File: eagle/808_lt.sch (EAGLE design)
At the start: 54 parts, among them IC1 TL071P, IC2 TL072P, Q1 2N3904, Q2 2N3906, Q3 2N3904, SW8 MSS42_SW_4PDT

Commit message: board started
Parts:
- removed VR10: 100KA, TR808clone:POT_808
- removed VR11: 500R, TR808clone:POT_8089MM
- R216: device TR808clone:R-EU_0207/5V -> TR808clone:R-EU_0207/7
- renumbered R1 to R3, R2 to R4
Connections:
- net GND: now also PINK_NOISE.RING; no longer VR10G$2.C, VR11G$2.C

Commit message: closer
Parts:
- added OUT_NORM, PINK_NORM: 22-23-2021, con-molex:22-23-2021
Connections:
- new net N$3: OUTPUT.NORM, OUT_NORM-1.S
- new net N$4: PINK_NOISE.NORM, PINK_NORM-1.S
- net GND: now also OUT_NORM-2.S, PINK_NORM-2.S, SW8G$4.S; no longer SW8G$2.S
- net N$111: now also SW8G$4.P; no longer SW8G$2.P
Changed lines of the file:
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@@
 <part name="R3" library="pot" deviceset="3RP/1610N" device="" value="100k"/>
 <part name="R4" library="pot" deviceset="3RP/1610N" device="" value="500R"/>
+<part name="PINK_NORM" library="con-molex" deviceset="22-23-2021" device=""/>
+<part name="OUT_NORM" library="con-molex" deviceset="22-23-2021" device=""/>
+<part name="V4" library="supply1" deviceset="GND" device=""/>
+<part name="V5" library="supply1" deviceset="GND" device=""/>
 </parts>
 <sheets>
@@
 <instance part="V54" gate="1" x="22.86" y="50.8"/>
 <instance part="SW8" gate="G$1" x="116.84" y="20.32" rot="MR180"/>
-<instance part="SW8" gate="G$2" x="35.56" y="30.48" rot="MR270"/>
 <instance part="SW8" gate="G$3" x="73.66" y="73.66" rot="MR0"/>
 <instance part="Q1" gate="G1" x="7.62" y="10.16"/>
@@
 <instance part="R3" gate="G$1" x="119.38" y="86.36" rot="R270"/>
 <instance part="R4" gate="G$1" x="38.1" y="71.12" rot="R90"/>
+<instance part="SW8" gate="G$4" x="35.56" y="30.48" rot="MR270"/>
+<instance part="PINK_NORM" gate="-1" x="-12.7" y="10.16" rot="R180"/>
+<instance part="PINK_NORM" gate="-2" x="-12.7" y="12.7" rot="R180"/>
+<instance part="OUT_NORM" gate="-1" x="142.24" y="58.42"/>
+<instance part="OUT_NORM" gate="-2" x="142.24" y="55.88"/>
+<instance part="V4" gate="1" x="-2.54" y="7.62"/>
+<instance part="V5" gate="1" x="137.16" y="50.8"/>
 </instances>
 <busses>
@@
 <pinref part="V159" gate="1" pin="GND"/>
 <wire x1="30.48" y1="25.4" x2="30.48" y2="22.86" width="0.1524" layer="91"/>
-<pinref part="SW8" gate="G$2" pin="S"/>
+<pinref part="SW8" gate="G$4" pin="S"/>
 </segment>
 <segment>
@@
 <pinref part="V3" gate="1" pin="GND"/>
 </segment>
+<segment>
+<pinref part="OUT_NORM" gate="-2" pin="S"/>
+<pinref part="V5" gate="1" pin="GND"/>
+<wire x1="139.7" y1="55.88" x2="137.16" y2="55.88" width="0.1524" layer="91"/>
+<wire x1="137.16" y1="55.88" x2="137.16" y2="53.34" width="0.1524" layer="91"/>
+</segment>
+<segment>
+<pinref part="PINK_NORM" gate="-2" pin="S"/>
+<pinref part="V4" gate="1" pin="GND"/>
+<wire x1="-10.16" y1="12.7" x2="-2.54" y2="12.7" width="0.1524" layer="91"/>
+<wire x1="-2.54" y1="12.7" x2="-2.54" y2="10.16" width="0.1524" layer="91"/>
+</segment>
 </net>
 <net name="N$111" class="0">
@@
 <pinref part="R224" gate="G$1" pin="1"/>
 <wire x1="40.64" y1="27.94" x2="43.18" y2="30.48" width="0.1524" layer="91"/>
-<pinref part="SW8" gate="G$2" pin="P"/>
+<pinref part="SW8" gate="G$4" pin="P"/>
 </segment>
 </net>
@@
 </segment>
 </net>
+<net name="N$3" class="0">
+<segment>
+<pinref part="OUT_NORM" gate="-1" pin="S"/>
+<wire x1="139.7" y1="58.42" x2="137.16" y2="58.42" width="0.1524" layer="91"/>
+<wire x1="137.16" y1="58.42" x2="137.16" y2="76.2" width="0.1524" layer="91"/>
+<pinref part="OUTPUT" gate="G$1" pin="NORM"/>
+<wire x1="137.16" y1="76.2" x2="142.24" y2="76.2" width="0.1524" layer="91"/>
+</segment>
+</net>
+<net name="N$4" class="0">
+<segment>
+<pinref part="PINK_NOISE" gate="G$1" pin="NORM"/>
+<wire x1="-10.16" y1="-2.54" x2="-7.62" y2="-2.54" width="0.1524" layer="91"/>
+<wire x1="-7.62" y1="-2.54" x2="-7.62" y2="10.16" width="0.1524" layer="91"/>
+<pinref part="PINK_NORM" gate="-1" pin="S"/>
+<wire x1="-7.62" y1="10.16" x2="-10.16" y2="10.16" width="0.1524" layer="91"/>
+</segment>
+</net>

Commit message: routed
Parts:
- renumbered R3 to LEVEL, R4 to TUNE
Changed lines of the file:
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@@
 <part name="PINK_NOISE" library="erthenvar" deviceset="AUDIO-JACK" device=""/>
 <part name="V3" library="supply1" deviceset="GND" device=""/>
-<part name="R3" library="pot" deviceset="3RP/1610N" device="" value="100k"/>
-<part name="R4" library="pot" deviceset="3RP/1610N" device="" value="500R"/>
+<part name="LEVEL" library="pot" deviceset="3RP/1610N" device="" value="100k"/>
+<part name="TUNE" library="pot" deviceset="3RP/1610N" device="" value="500R"/>
 <part name="PINK_NORM" library="con-molex" deviceset="22-23-2021" device=""/>
 <part name="OUT_NORM" library="con-molex" deviceset="22-23-2021" device=""/>
@@
 <instance part="PINK_NOISE" gate="G$1" x="-17.78" y="-2.54" rot="MR180"/>
 <instance part="V3" gate="1" x="-10.16" y="-7.62"/>
-<instance part="R3" gate="G$1" x="119.38" y="86.36" rot="R270"/>
-<instance part="R4" gate="G$1" x="38.1" y="71.12" rot="R90"/>
+<instance part="LEVEL" gate="G$1" x="119.38" y="86.36" rot="R270"/>
+<instance part="TUNE" gate="G$1" x="38.1" y="71.12" rot="R90"/>
 <instance part="SW8" gate="G$4" x="35.56" y="30.48" rot="MR270"/>
 <instance part="PINK_NORM" gate="-1" x="-12.7" y="10.16" rot="R180"/>
@@
 <pinref part="D81" gate="G$1" pin="A"/>
 <pinref part="D80" gate="G$1" pin="C"/>
-<pinref part="R4" gate="G$1" pin="A"/>
+<pinref part="TUNE" gate="G$1" pin="A"/>
 </segment>
 </net>
@@
 <wire x1="38.1" y1="78.74" x2="38.1" y2="76.2" width="0.1524" layer="91"/>
 <pinref part="R231" gate="G$1" pin="1"/>
-<pinref part="R4" gate="G$1" pin="S"/>
+<pinref part="TUNE" gate="G$1" pin="S"/>
 </segment>
 </net>
@@
 <pinref part="IC1" gate="A" pin="-IN"/>
 <junction x="114.3" y="50.8"/>
-<pinref part="R3" gate="G$1" pin="A"/>
+<pinref part="LEVEL" gate="G$1" pin="A"/>
 </segment>
 </net>
@@
 <wire x1="119.38" y1="81.28" x2="121.92" y2="81.28" width="0.1524" layer="91"/>
 <pinref part="C82" gate="G$1" pin="-"/>
-<pinref part="R3" gate="G$1" pin="S"/>
+<pinref part="LEVEL" gate="G$1" pin="S"/>
 </segment>
 </net>
@@
 <wire x1="33.02" y1="71.12" x2="30.48" y2="71.12" width="0.1524" layer="91"/>
 <pinref part="V148" gate="1" pin="GND"/>
-<pinref part="R4" gate="G$1" pin="E"/>
-</segment>
-<segment>
+<pinref part="TUNE" gate="G$1" pin="E"/>
+</segment>
+<segment>

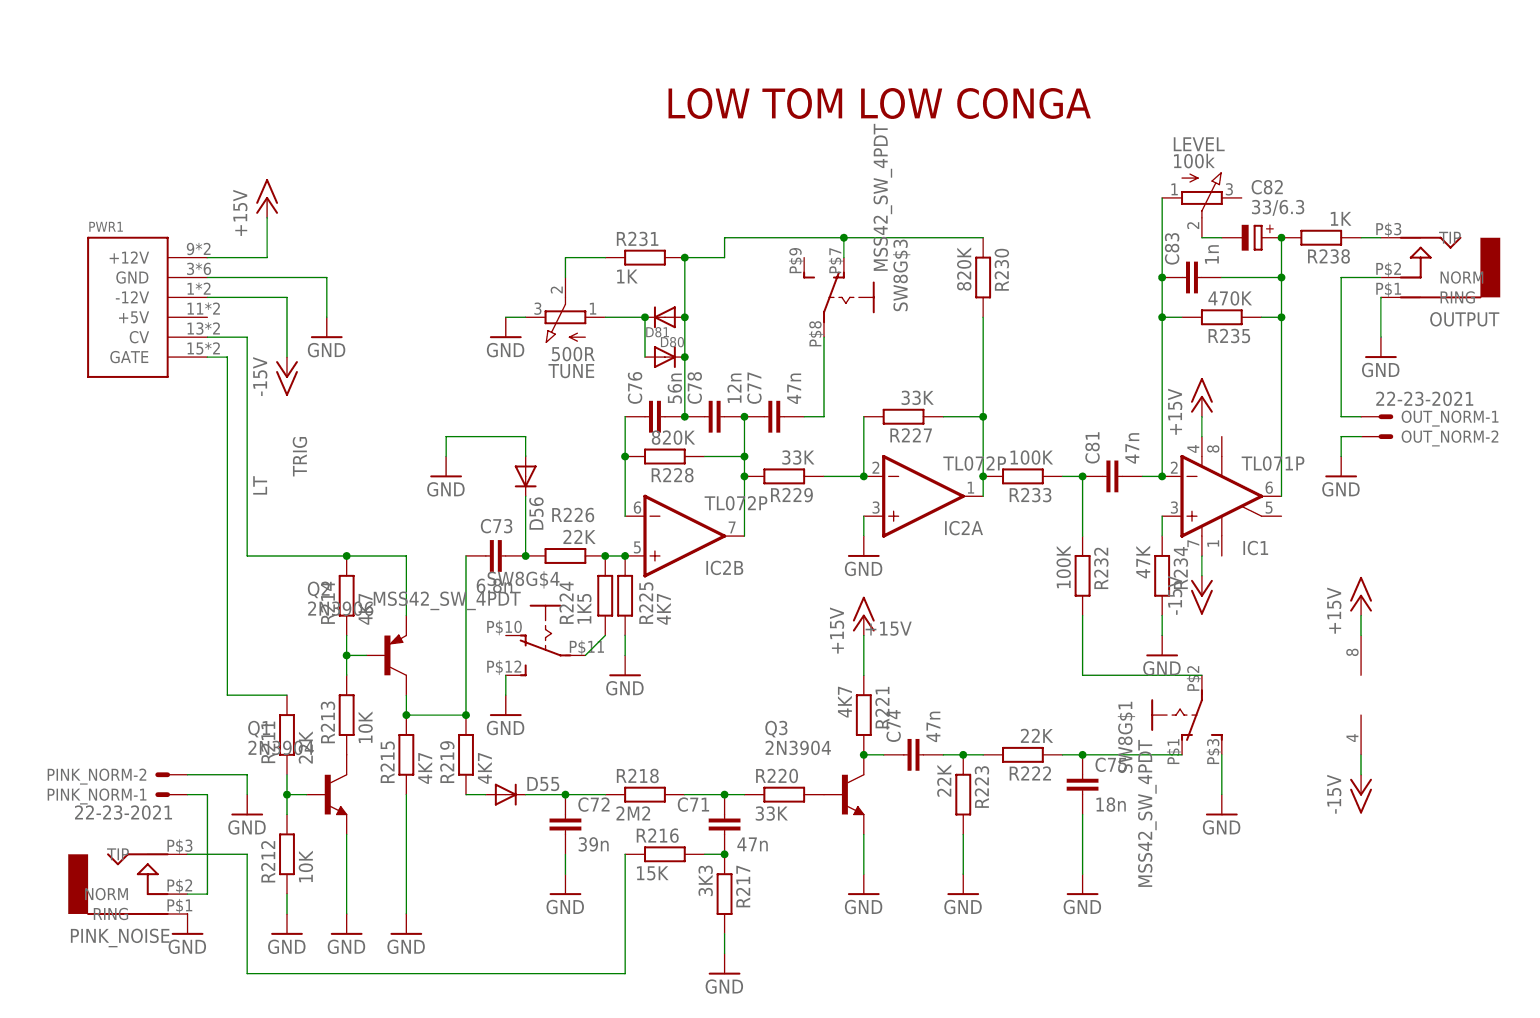
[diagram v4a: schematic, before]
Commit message: corrected 071 power and added resistors to tune pot for value change
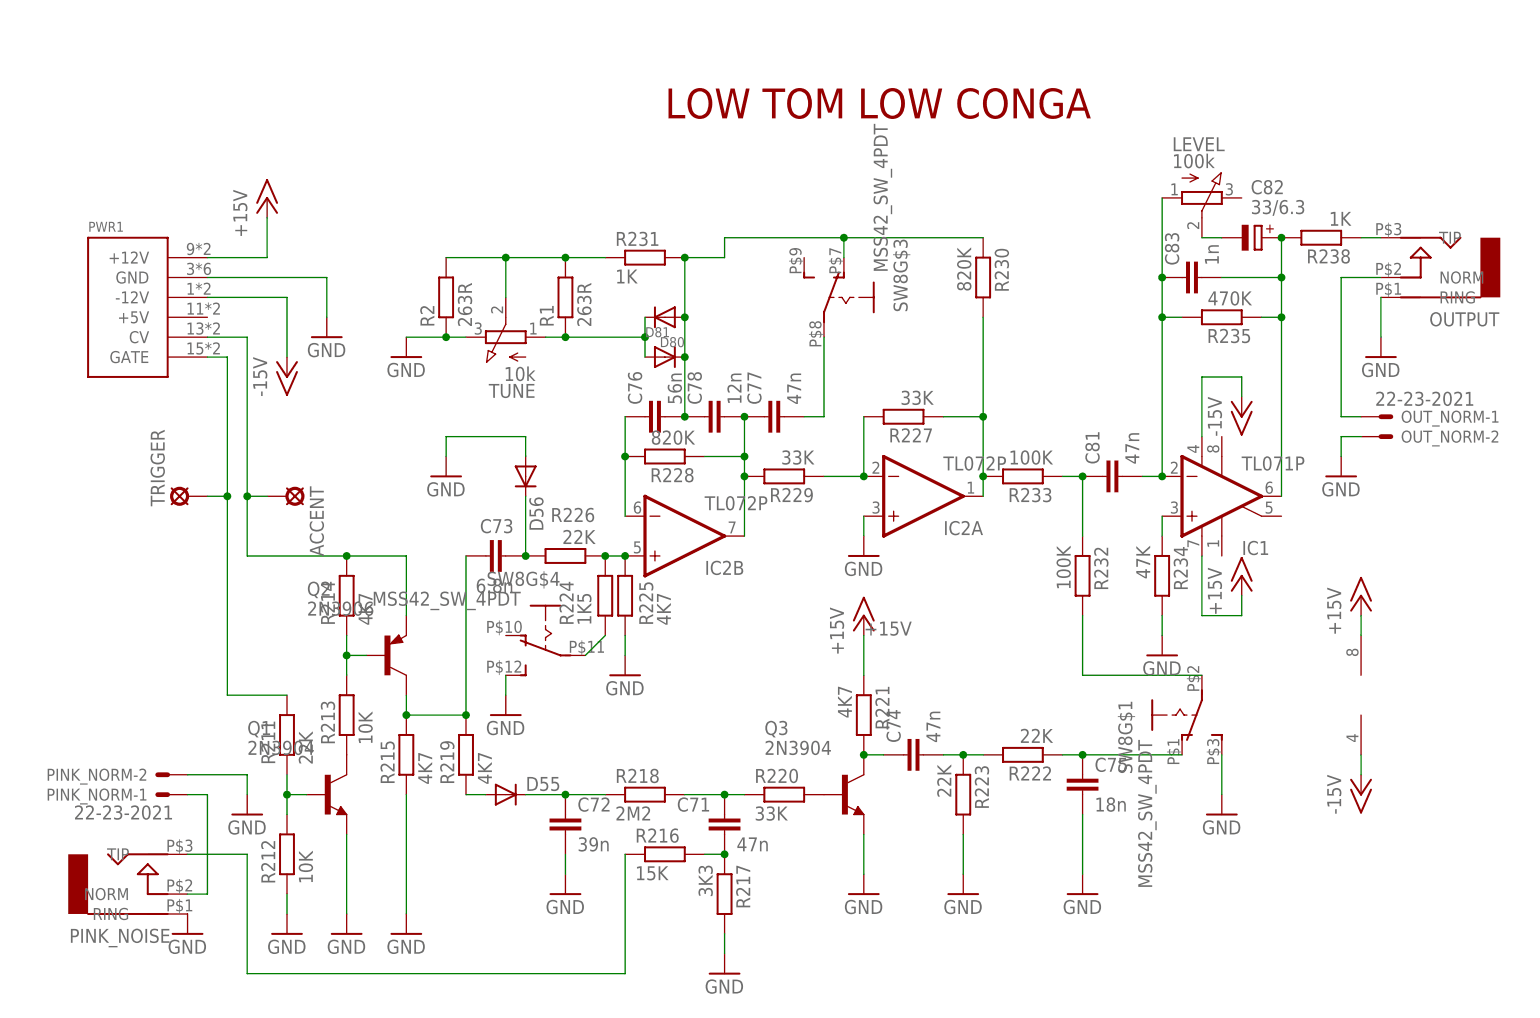
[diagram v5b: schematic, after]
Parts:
- added ACCENT, TRIGGER: LSP10, solpad:LSP10
- added R1, R2: 263R, TR808clone:R-EU_0207/7
- TUNE: value 500R -> 10k
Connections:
- net +15V: now also IC1.V+; no longer IC1.V-
- net -15V: now also IC1.V-; no longer IC1.V+
- net GND: now also R2.1
- net LT: now also TRIGGER.MP
- net N$254: now also R1.1
- net N$255: now also R1.2, R2.2
- net TRIG: now also ACCENT.MP
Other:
- moved on the sheet: TUNE
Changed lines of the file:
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@@
 <part name="V3" library="supply1" deviceset="GND" device=""/>
 <part name="LEVEL" library="pot" deviceset="3RP/1610N" device="" value="100k"/>
-<part name="TUNE" library="pot" deviceset="3RP/1610N" device="" value="500R"/>
+<part name="TUNE" library="pot" deviceset="3RP/1610N" device="" value="10k"/>
 <part name="PINK_NORM" library="con-molex" deviceset="22-23-2021" device=""/>
 <part name="OUT_NORM" library="con-molex" deviceset="22-23-2021" device=""/>
 <part name="V4" library="supply1" deviceset="GND" device=""/>
 <part name="V5" library="supply1" deviceset="GND" device=""/>
+<part name="R1" library="TR808clone" deviceset="R-EU_" device="0207/7" value="263R"/>
+<part name="R2" library="TR808clone" deviceset="R-EU_" device="0207/7" value="263R"/>
+<part name="TRIGGER" library="solpad" deviceset="LSP10" device=""/>
+<part name="ACCENT" library="solpad" deviceset="LSP10" device=""/>
 </parts>
 <sheets>
@@
 <instance part="R227" gate="G$1" x="81.28" y="58.42" rot="R180"/>
 <instance part="R231" gate="G$1" x="48.26" y="78.74"/>
-<instance part="V148" gate="1" x="30.48" y="68.58"/>
+<instance part="V148" gate="1" x="17.78" y="66.04"/>
 <instance part="V149" gate="1" x="76.2" y="40.64"/>
 <instance part="R233" gate="G$1" x="96.52" y="50.8" rot="R180"/>
@@
 <instance part="P-1" gate="1" x="2.54" y="63.5"/>
 <instance part="V1" gate="1" x="7.62" y="68.58"/>
-<instance part="P+2" gate="1" x="119.38" y="60.96"/>
-<instance part="P-2" gate="1" x="119.38" y="35.56"/>
+<instance part="P+2" gate="1" x="124.46" y="38.1"/>
+<instance part="P-2" gate="1" x="124.46" y="58.42"/>
 <instance part="IC2" gate="A" x="83.82" y="48.26" rot="MR180"/>
 <instance part="IC2" gate="B" x="53.34" y="43.18" rot="MR180"/>
@@
 <instance part="V3" gate="1" x="-10.16" y="-7.62"/>
 <instance part="LEVEL" gate="G$1" x="119.38" y="86.36" rot="R270"/>
-<instance part="TUNE" gate="G$1" x="38.1" y="71.12" rot="R90"/>
+<instance part="TUNE" gate="G$1" x="30.48" y="68.58" rot="R90"/>
 <instance part="SW8" gate="G$4" x="35.56" y="30.48" rot="MR270"/>
 <instance part="PINK_NORM" gate="-1" x="-12.7" y="10.16" rot="R180"/>
@@
 <instance part="V4" gate="1" x="-2.54" y="7.62"/>
 <instance part="V5" gate="1" x="137.16" y="50.8"/>
+<instance part="R1" gate="G$1" x="38.1" y="73.66" rot="R90"/>
+<instance part="R2" gate="G$1" x="22.86" y="73.66" rot="R90"/>
+<instance part="TRIGGER" gate="1" x="-10.16" y="48.26" rot="R90"/>
+<instance part="ACCENT" gate="1" x="2.54" y="48.26" rot="R270"/>
 </instances>
 <busses>
@@
 <net name="N$254" class="0">
 <segment>
-<wire x1="48.26" y1="71.12" x2="48.26" y2="66.04" width="0.1524" layer="91"/>
-<wire x1="48.26" y1="71.12" x2="43.18" y2="71.12" width="0.1524" layer="91"/>
-<junction x="48.26" y="71.12"/>
+<wire x1="48.26" y1="71.12" x2="48.26" y2="68.58" width="0.1524" layer="91"/>
 <pinref part="D81" gate="G$1" pin="A"/>
 <pinref part="D80" gate="G$1" pin="C"/>
 <pinref part="TUNE" gate="G$1" pin="A"/>
+<wire x1="48.26" y1="68.58" x2="48.26" y2="66.04" width="0.1524" layer="91"/>
+<wire x1="35.56" y1="68.58" x2="38.1" y2="68.58" width="0.1524" layer="91"/>
+<junction x="48.26" y="68.58"/>
+<pinref part="R1" gate="G$1" pin="1"/>
+<wire x1="38.1" y1="68.58" x2="48.26" y2="68.58" width="0.1524" layer="91"/>
+<junction x="38.1" y="68.58"/>
 </segment>
 </net>
@@
 <segment>
 <wire x1="43.18" y1="78.74" x2="38.1" y2="78.74" width="0.1524" layer="91"/>
-<wire x1="38.1" y1="78.74" x2="38.1" y2="76.2" width="0.1524" layer="91"/>
+<wire x1="38.1" y1="78.74" x2="30.48" y2="78.74" width="0.1524" layer="91"/>
+<wire x1="30.48" y1="78.74" x2="30.48" y2="73.66" width="0.1524" layer="91"/>
 <pinref part="R231" gate="G$1" pin="1"/>
 <pinref part="TUNE" gate="G$1" pin="S"/>
+<pinref part="R1" gate="G$1" pin="2"/>
+<junction x="38.1" y="78.74"/>
+<pinref part="R2" gate="G$1" pin="2"/>
+<wire x1="30.48" y1="78.74" x2="22.86" y2="78.74" width="0.1524" layer="91"/>
+<junction x="30.48" y="78.74"/>
 </segment>
 </net>
@@
 <segment>
 <pinref part="R211" gate="G$1" pin="2"/>
-<label x="0" y="48.26" size="1.778" layer="95" rot="R90"/>
 <pinref part="PWR1" gate="G$1" pin="GATE"/>
 <wire x1="-7.62" y1="66.04" x2="-5.08" y2="66.04" width="0.1524" layer="91"/>
-<wire x1="-5.08" y1="66.04" x2="-5.08" y2="22.86" width="0.1524" layer="91"/>
+<wire x1="-5.08" y1="66.04" x2="-5.08" y2="48.26" width="0.1524" layer="91"/>
+<wire x1="-5.08" y1="48.26" x2="-5.08" y2="22.86" width="0.1524" layer="91"/>
 <wire x1="-5.08" y1="22.86" x2="2.54" y2="22.86" width="0.1524" layer="91"/>
+<pinref part="TRIGGER" gate="1" pin="MP"/>
+<wire x1="-7.62" y1="48.26" x2="-5.08" y2="48.26" width="0.1524" layer="91"/>
+<junction x="-5.08" y="48.26"/>
 </segment>
 </net>
@@
 <junction x="10.16" y="40.64"/>
 <pinref part="R214" gate="G$1" pin="2"/>
-<label x="5.08" y="50.8" size="1.778" layer="95" rot="R90"/>
 <pinref part="Q2" gate="G$1" pin="E"/>
 <wire x1="10.16" y1="40.64" x2="-2.54" y2="40.64" width="0.1524" layer="91"/>
-<wire x1="-2.54" y1="40.64" x2="-2.54" y2="68.58" width="0.1524" layer="91"/>
+<wire x1="-2.54" y1="40.64" x2="-2.54" y2="48.26" width="0.1524" layer="91"/>
 <pinref part="PWR1" gate="G$1" pin="CV"/>
+<wire x1="-2.54" y1="48.26" x2="-2.54" y2="68.58" width="0.1524" layer="91"/>
 <wire x1="-2.54" y1="68.58" x2="-7.62" y2="68.58" width="0.1524" layer="91"/>
+<pinref part="ACCENT" gate="1" pin="MP"/>
+<wire x1="0" y1="48.26" x2="-2.54" y2="48.26" width="0.1524" layer="91"/>
+<junction x="-2.54" y="48.26"/>
 </segment>
 </net>
@@
 </segment>
 <segment>
-<wire x1="33.02" y1="71.12" x2="30.48" y2="71.12" width="0.1524" layer="91"/>
+<wire x1="25.4" y1="68.58" x2="22.86" y2="68.58" width="0.1524" layer="91"/>
 <pinref part="V148" gate="1" pin="GND"/>
 <pinref part="TUNE" gate="G$1" pin="E"/>
+<pinref part="R2" gate="G$1" pin="1"/>
+<wire x1="22.86" y1="68.58" x2="17.78" y2="68.58" width="0.1524" layer="91"/>
+<junction x="22.86" y="68.58"/>
 </segment>
 <segment>
@@
 </segment>
 <segment>
-<pinref part="IC1" gate="A" pin="V-"/>
-<pinref part="P+2" gate="1" pin="+15V"/>
-<wire x1="119.38" y1="58.42" x2="119.38" y2="55.88" width="0.1524" layer="91"/>
-</segment>
-<segment>
 <pinref part="IC2" gate="P" pin="V+"/>
 <pinref part="P+3" gate="1" pin="+15V"/>
@@
 <pinref part="P+4" gate="1" pin="+15V"/>
 </segment>
+<segment>
+<pinref part="P+2" gate="1" pin="+15V"/>
+<wire x1="124.46" y1="35.56" x2="124.46" y2="33.02" width="0.1524" layer="91"/>
+<pinref part="IC1" gate="A" pin="V+"/>
+<wire x1="124.46" y1="33.02" x2="119.38" y2="33.02" width="0.1524" layer="91"/>
+<wire x1="119.38" y1="33.02" x2="119.38" y2="40.64" width="0.1524" layer="91"/>
+</segment>
 </net>
 <net name="-15V" class="0">
@@
 </segment>
 <segment>
-<pinref part="IC1" gate="A" pin="V+"/>
-<pinref part="P-2" gate="1" pin="-15V"/>
-<wire x1="119.38" y1="38.1" x2="119.38" y2="40.64" width="0.1524" layer="91"/>
-</segment>
-<segment>
 <pinref part="IC2" gate="P" pin="V-"/>
 <pinref part="P-3" gate="1" pin="-15V"/>
 <wire x1="139.7" y1="12.7" x2="139.7" y2="15.24" width="0.1524" layer="91"/>
 </segment>
-</net>
+<segment>
+<pinref part="IC1" gate="A" pin="V-"/>
+<wire x1="119.38" y1="55.88" x2="119.38" y2="63.5" width="0.1524" layer="91"/>
+<pinref part="P-2" gate="1" pin="-15V"/>
+<wire x1="119.38" y1="63.5" x2="124.46" y2="63.5" width="0.1524" layer="91"/>
+<wire x1="124.46" y1="63.5" x2="124.46" y2="60.96" width="0.1524" layer="91"/>
+</segment>
+</net>
